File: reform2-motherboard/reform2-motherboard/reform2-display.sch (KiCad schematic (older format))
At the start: 5 parts, among them J2 EDP_30, U10 SN65DSI86ZQER

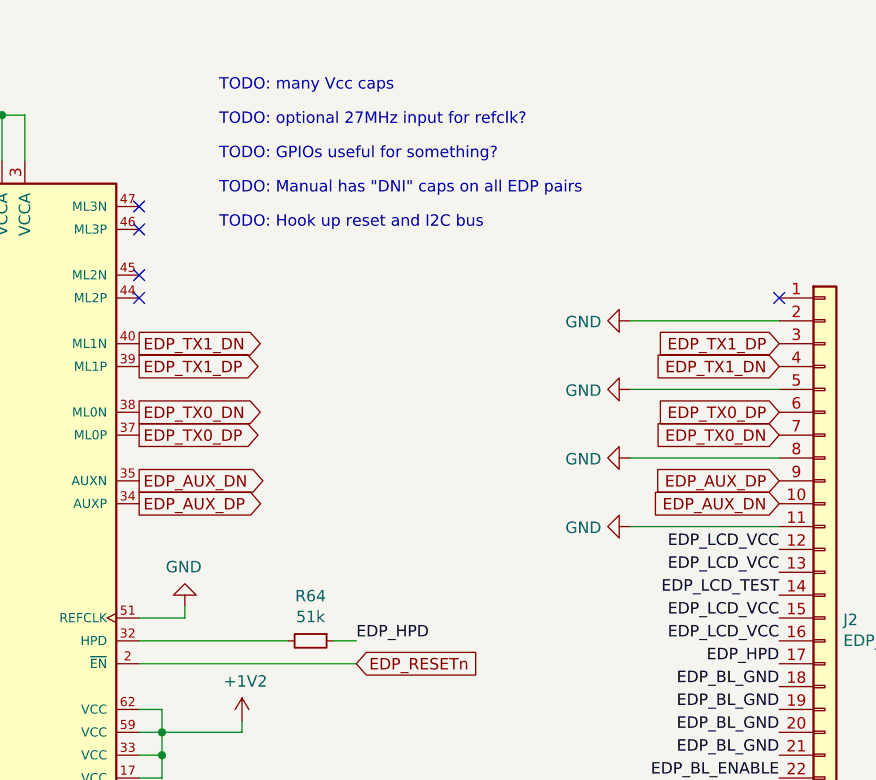
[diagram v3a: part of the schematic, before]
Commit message: WIP: reform2 schematic detail work all over the board and more footprints and 3d models added; changed one mpcie to M.2/NGFF/NVMe
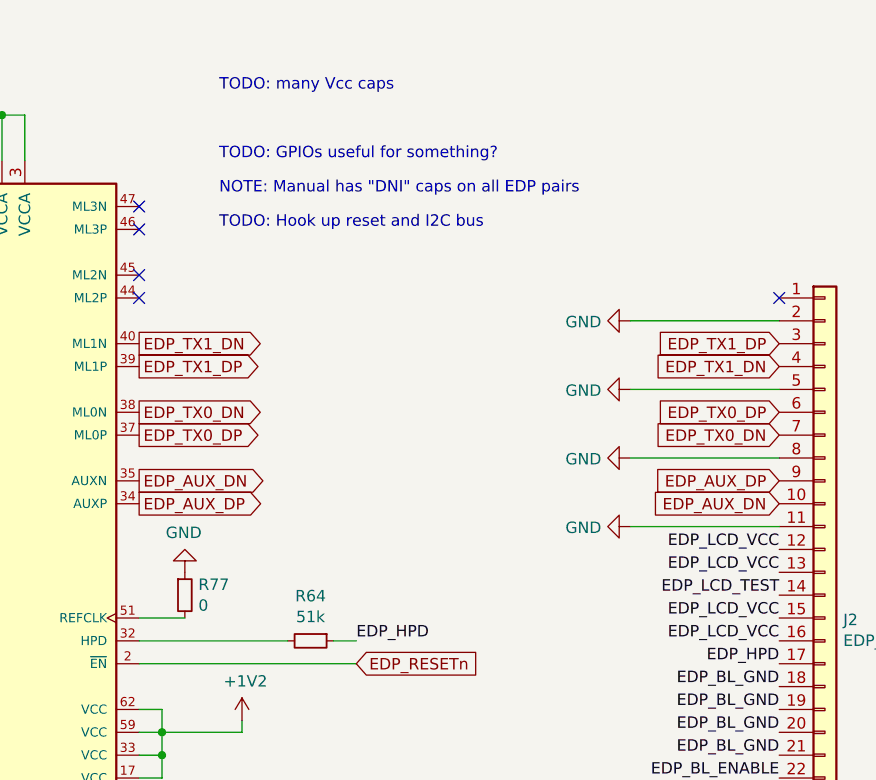
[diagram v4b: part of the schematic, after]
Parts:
- added R77: 0, Button_Switch_SMD:SW_Push_1P1T_NO_CK_KMR2, symbol Device:R_Small
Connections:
- net GND: now also R77.1; no longer U10.51 (REFCLK)
- new net: R77.2, U10.51 (REFCLK)
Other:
- note added: "NOTE: Manual has "DNI" caps on all EDP pairs"
- note removed: "TODO: Manual has "DNI" caps on all EDP pairs"
- note removed: "TODO: optional 27MHz input for refclk?"
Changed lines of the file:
@@
 L power:GND #PWR038
 U 1 1 5DAA7616
-P 6100 3600
-F 0 "#PWR038" H 6100 3350 50  0001 C CNN
-F 1 "GND" H 6105 3427 50  0000 C CNN
-F 2 "" H 6100 3600 50  0001 C CNN
-F 3 "" H 6100 3600 50  0001 C CNN
-	1    6100 3600
+P 6100 3450
+F 0 "#PWR038" H 6100 3200 50  0001 C CNN
+F 1 "GND" H 6105 3277 50  0000 C CNN
+F 2 "" H 6100 3450 50  0001 C CNN
+F 3 "" H 6100 3450 50  0001 C CNN
+	1    6100 3450
 	-1   0    0    1
 $EndComp
 Wire Wire Line
-	6100 3600 6100 3650
-Wire Wire Line
 	6100 3650 5900 3650
-Text Notes 6250 1500 0    50   ~ 0
-TODO: optional 27MHz input for refclk?
 Text GLabel 6850 3850 2    50   Input ~ 0
 EDP_RESETn
@@
 	7500 5050 6950 5050
 Text Notes 6250 1800 0    50   ~ 0
-TODO: Manual has "DNI" caps on all EDP pairs
+NOTE: Manual has "DNI" caps on all EDP pairs
 Text Notes 6250 1950 0    50   ~ 0
 TODO: Hook up reset and I2C bus
+$Comp
+L Device:R_Small R77
+U 1 1 60F2545C
+P 6100 3550
+F 0 "R77" H 6159 3596 50  0000 L CNN
+F 1 "0" H 6159 3505 50  0000 L CNN
+F 2 "Button_Switch_SMD:SW_Push_1P1T_NO_CK_KMR2" H 6100 3550 50  0001 C CNN
+F 3 "~" H 6100 3550 50  0001 C CNN
+	1    6100 3550
+	1    0    0    -1
+$EndComp
 $EndSCHEMATC

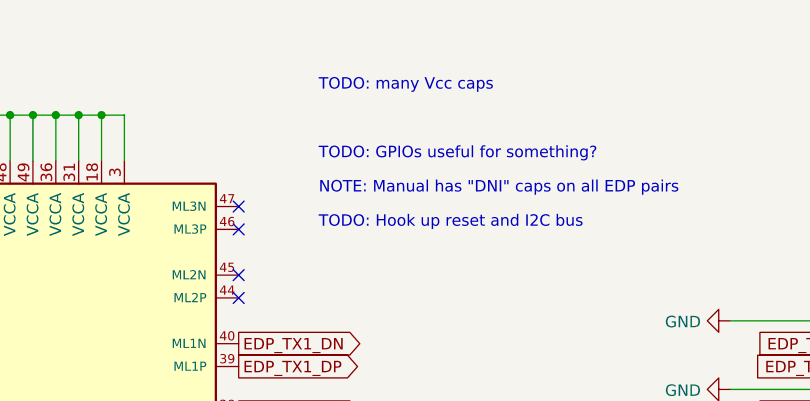
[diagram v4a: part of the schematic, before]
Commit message: WIP reform2: motherboard: many components sanity checked, passives footprints, fixed wrong NVMe/M.2 connector symbol and pins
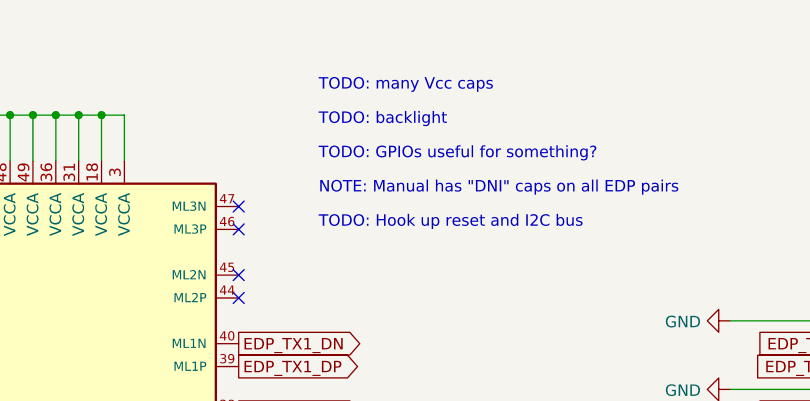
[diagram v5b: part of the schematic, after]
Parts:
- R77: footprint Button_Switch_SMD:SW_Push_1P1T_NO_CK_KMR2 -> Resistor_SMD:R_0603_1608Metric
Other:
- note added: "TODO: backlight"
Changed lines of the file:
@@
 F 0 "R77" H 6159 3596 50  0000 L CNN
 F 1 "0" H 6159 3505 50  0000 L CNN
-F 2 "Button_Switch_SMD:SW_Push_1P1T_NO_CK_KMR2" H 6100 3550 50  0001 C CNN
+F 2 "Resistor_SMD:R_0603_1608Metric" H 6100 3550 50  0001 C CNN
 F 3 "~" H 6100 3550 50  0001 C CNN
 	1    6100 3550
 	1    0    0    -1
 $EndComp
+Text Notes 6250 1500 0    50   ~ 0
+TODO: backlight
 $EndSCHEMATC

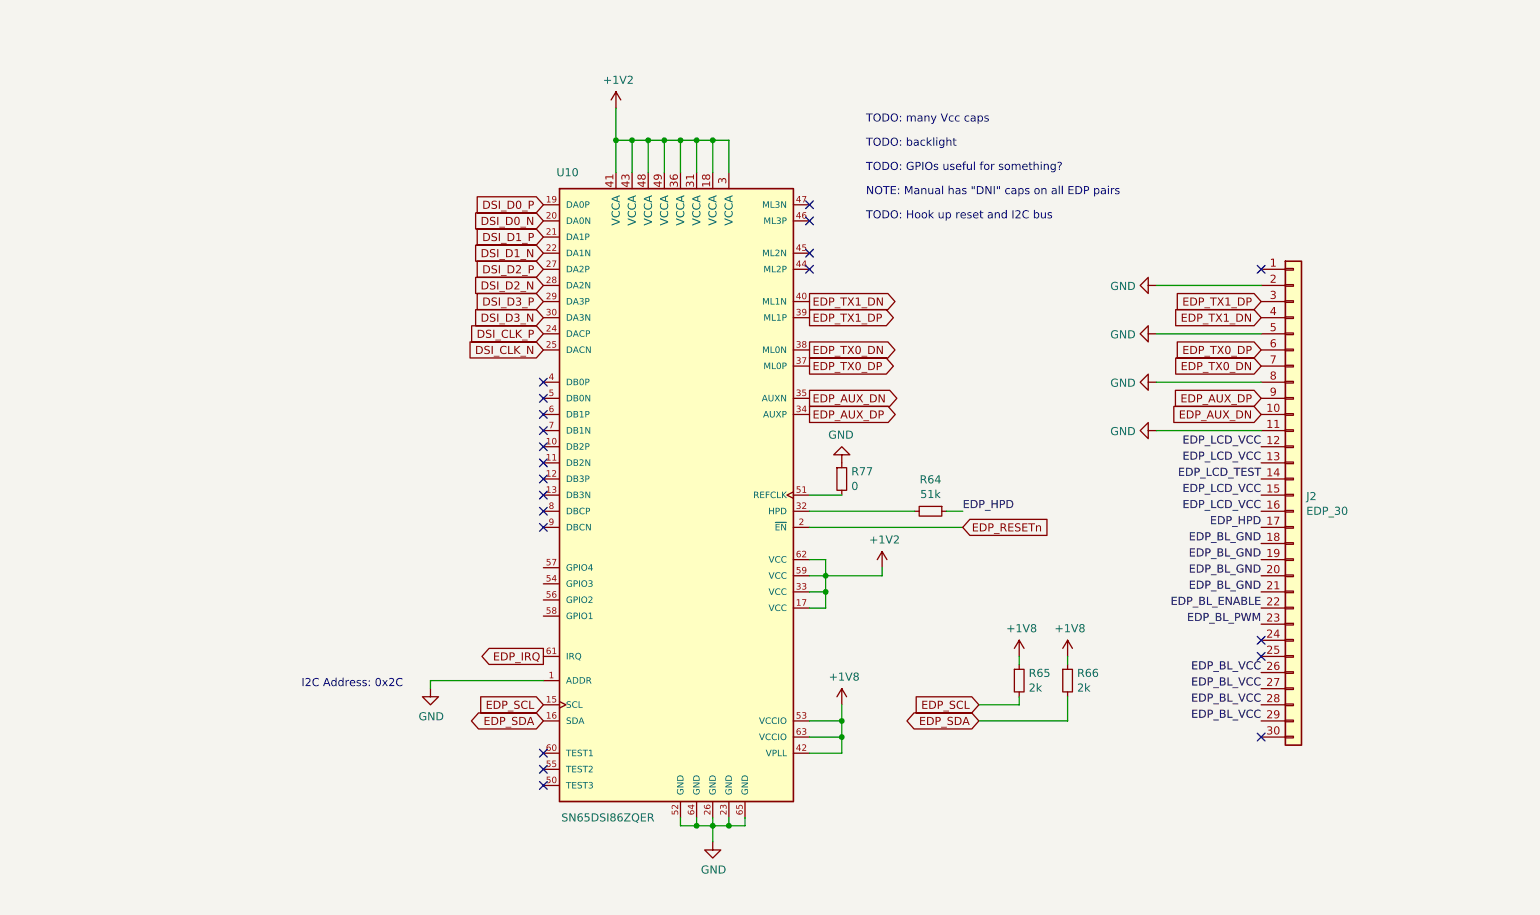
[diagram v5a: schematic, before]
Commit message: WIP: reform2 motherboard: eDP/eDP bridge caps
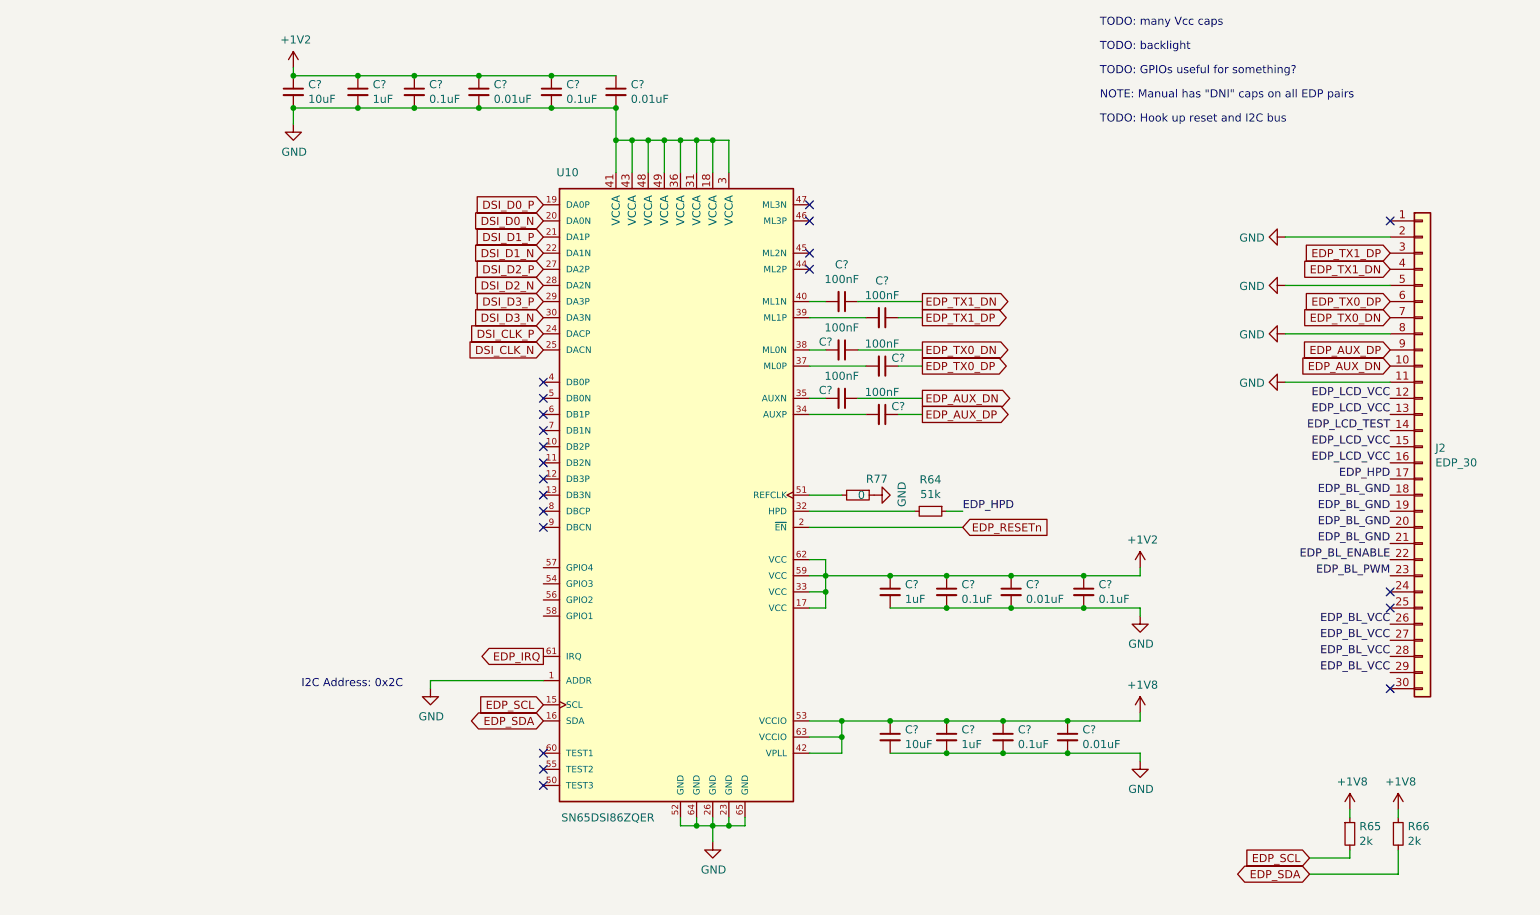
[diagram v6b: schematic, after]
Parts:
- added C? (x5): 0.1uF, symbol Device:C_Small
- added C? (x4): 0.01uF, symbol Device:C_Small
- added C? (x3): 1uF, symbol Device:C_Small
- added C? (x2): 10uF, symbol Device:C_Small
- added C? (x6): 100nF, symbol Device:C_Small
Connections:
- net +1V2: now also C?.1, C?.1, C?.1, C?.1, C?.1, C?.1, C?.1, C?.1, C?.1, C?.1; no longer U10.18 (VCCA), U10.3 (VCCA), U10.31 (VCCA), U10.36 (VCCA), U10.41 (VCCA), U10.43 (VCCA), U10.48 (VCCA), U10.49 (VCCA)
- net +1V8: now also C?.1, C?.1, C?.1, C?.1
- net EDP_AUX_DN: now also C?.1; no longer U10.35 (AUXN)
- net EDP_AUX_DP: now also C?.1; no longer U10.34 (AUXP)
- net EDP_TX0_DN: now also C?.1; no longer U10.38 (ML0N)
- net EDP_TX0_DP: now also C?.1; no longer U10.37 (ML0P)
- net EDP_TX1_DN: now also C?.1; no longer U10.40 (ML1N)
- net EDP_TX1_DP: now also C?.1; no longer U10.39 (ML1P)
- net GND: now also U10.18 (VCCA), U10.3 (VCCA), U10.31 (VCCA), U10.36 (VCCA), U10.41 (VCCA), U10.43 (VCCA), U10.48 (VCCA), U10.49 (VCCA), C?.2, C?.2, C?.2, C?.2, C?.2, C?.2, C?.2, C?.2, C?.2, C?.2, C?.2, C?.2, C?.2, C?.2
- new net: C?.2, U10.34 (AUXP)
- new net: C?.2, U10.35 (AUXN)
- new net: C?.2, U10.37 (ML0P)
- new net: C?.2, U10.38 (ML0N)
- new net: C?.2, U10.39 (ML1P)
- new net: C?.2, U10.40 (ML1N)
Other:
- moved on the sheet: J2, R65, R66, R77

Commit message: WIP: reform2 motherboard: more sanity and footprint checks, passives
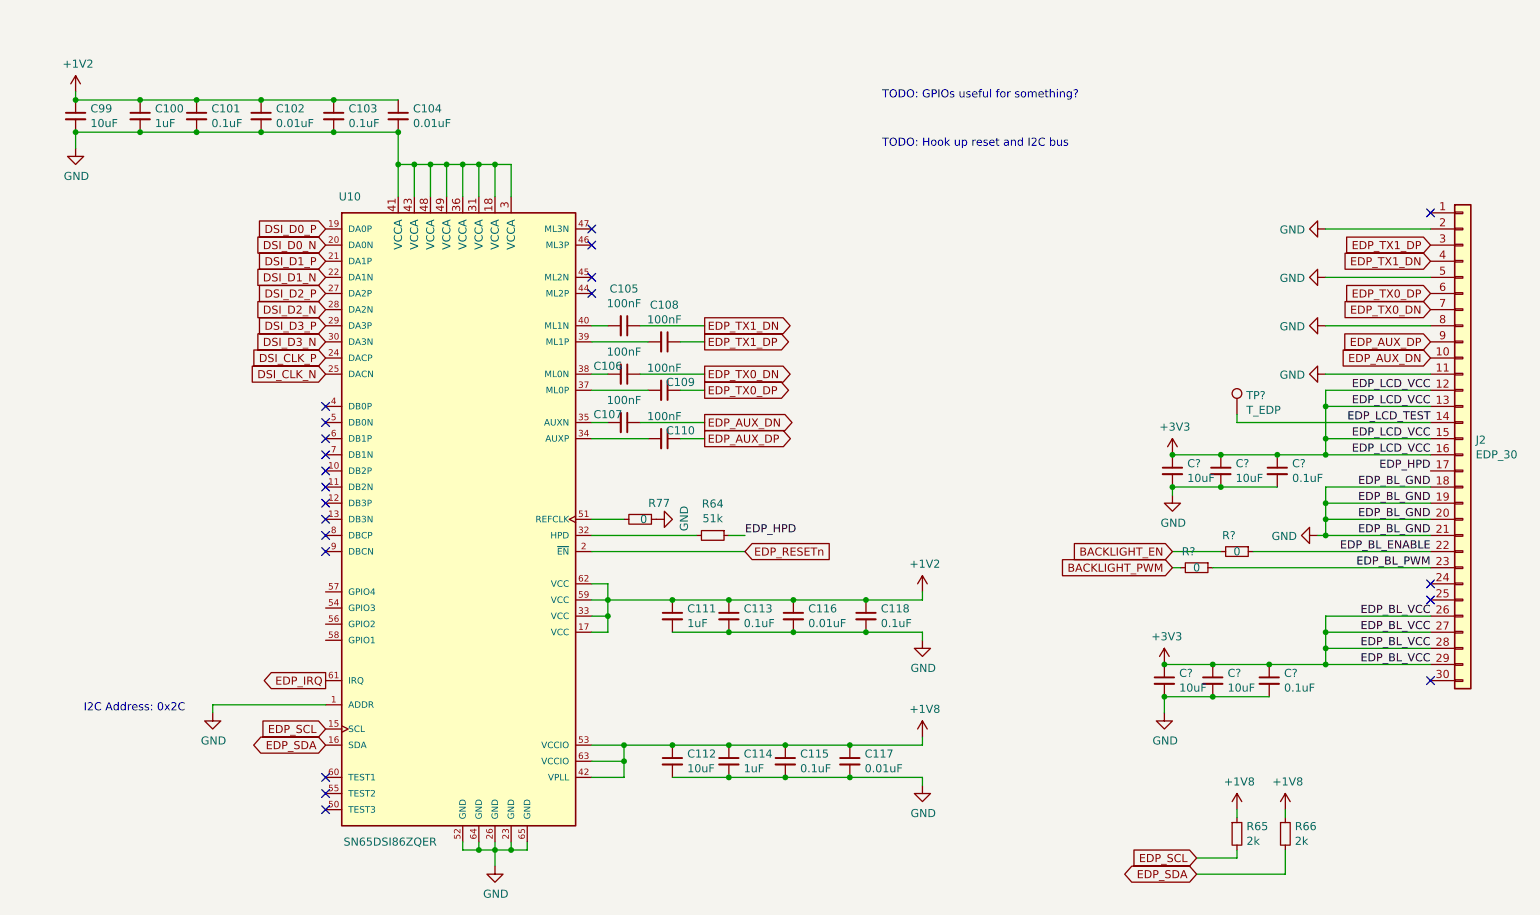
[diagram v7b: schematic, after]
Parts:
- added C? (x4): 10uF, symbol Device:C_Small
- added C? (x2): 0.1uF, symbol Device:C_Small
- added R? (x2): 0, symbol Device:R_Small
- added TP?: T_EDP, symbol Connector:TestPoint
- gave numbers to parts that had none: 20
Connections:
- net EDP_BL_GND is gone; now on net GND: J2.18 (Pin_18), J2.19 (Pin_19), J2.20 (Pin_20), J2.21 (Pin_21)
- net EDP_LCD_VCC is gone; now on net +3V3: J2.12 (Pin_12), J2.13 (Pin_13), J2.15 (Pin_15), J2.16 (Pin_16)
- net EDP_BL_ENABLE: now also R?.1
- net EDP_BL_PWM: now also R?.1
- net EDP_LCD_TEST: now also TP?.1
- net GND: now also C?.2, C?.2, C?.2, C?.2, C?.2, C?.2
- net EDP_BL_VCC renamed +3V3
- net +3V3: now also C?.1, C?.1, C?.1, C?.1, C?.1, C?.1
- new net BACKLIGHT_EN: R?.2
- new net BACKLIGHT_PWM: R?.2
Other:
- note removed: "NOTE: Manual has "DNI" caps on all EDP pairs"
- note removed: "TODO: backlight"
- note removed: "TODO: many Vcc caps"
- moved on the sheet: C100, C101, C102, C103, C104, C105, C106, C107, C108, C109, C110, C111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

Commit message: WIP: reform2 motherboard: more schematics tuning, preliminary selection of most components
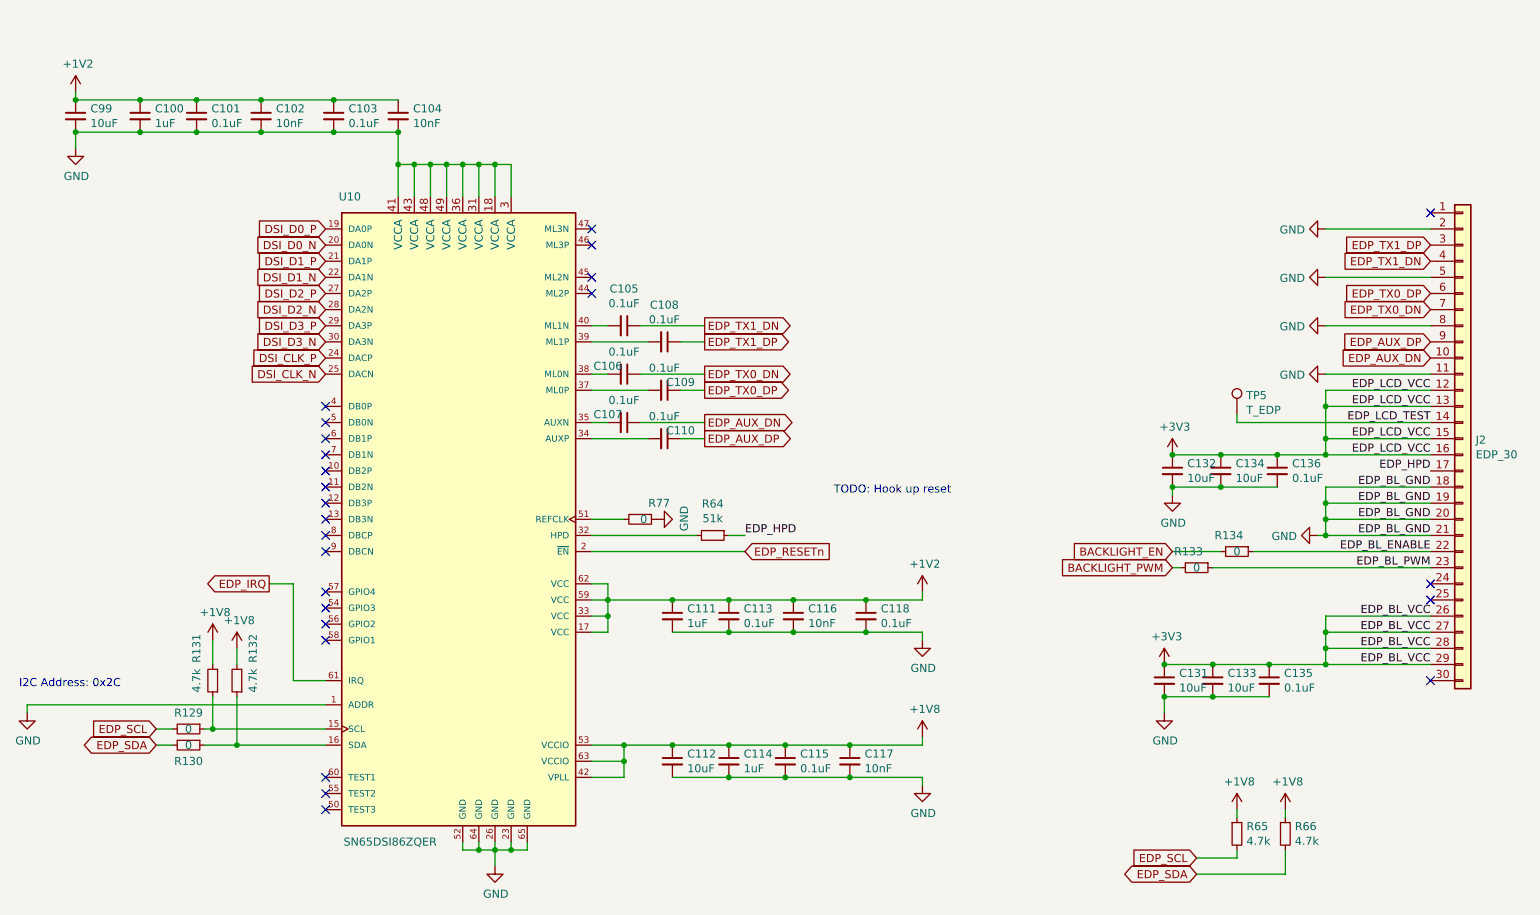
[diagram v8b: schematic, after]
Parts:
- added R129, R130: 0, Resistor_SMD:R_0603_1608Metric, symbol Device:R_Small
- added R131, R132: 4.7k, Resistor_SMD:R_0603_1608Metric, symbol Device:R_Small
- C100, C111, C114: footprint (none) -> Capacitor_SMD:C_0603_1608Metric; Manufacturer (none) -> Taiyo Yuden; Manufacturer_No (none) -> JMK107C6105KA
- C101, C103, C113, C115, C118: footprint (none) -> Capacitor_SMD:C_0603_1608Metric; Manufacturer (none) -> TDK; Manufacturer_No (none) -> CGA3E2X8R1E104K080AE
- C102, C104, C116, C117: value 0.01uF -> 10nF; footprint (none) -> Capacitor_SMD:C_0603_1608Metric; Manufacturer (none) -> KEMET; Manufacturer_No (none) -> C0603C103K5RAC3190
- C105, C106, C107, C108, C109, C110: value 100nF -> 0.1uF; footprint (none) -> Capacitor_SMD:C_0603_1608Metric; Manufacturer (none) -> TDK; Manufacturer_No (none) -> CGA3E2X8R1E104K080AE
- C112, C99: footprint (none) -> Capacitor_SMD:C_0603_1608Metric; Manufacturer (none) -> Taiyo Yuden; Manufacturer_No (none) -> LMK107BBJ106KALT
- C131, C132, C133, C134: renamed from C?; footprint (none) -> Capacitor_SMD:C_0603_1608Metric; Manufacturer (none) -> Taiyo Yuden; Manufacturer_No (none) -> LMK107BBJ106KALT
- C135, C136: renamed from C?; footprint (none) -> Capacitor_SMD:C_0603_1608Metric; Manufacturer (none) -> TDK; Manufacturer_No (none) -> CGA3E2X8R1E104K080AE
- J2: Manufacturer (none) -> Hirose; Manufacturer_No (none) -> FH12-30S-0.5SH(55)
- R133, R134: renamed from R?; footprint (none) -> Resistor_SMD:R_0603_1608Metric; Manufacturer (none) -> Vishay Dale; Manufacturer_No (none) -> CRCW06030000Z0EAC
- R65, R66: value 2k -> 4.7k; Manufacturer (none) -> Yageo; Manufacturer_No (none) -> RC0603FR-074K7L
- R77: Manufacturer (none) -> Vishay Dale; Manufacturer_No (none) -> CRCW06030000Z0EAC
- TP5: renamed from TP?; footprint (none) -> TestPoint:TestPoint_Pad_1.0x1.0mm
- U10: Manufacturer (none) -> Texas Instruments; Manufacturer_No (none) -> SN65DSI86ZQER
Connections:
- net +1V8: now also R131.2, R132.2
- net EDP_SCL: now also R129.2; no longer U10.15 (SCL)
- net EDP_SDA: now also R130.2; no longer U10.16 (SDA)
- new net: R129.1, R131.1, U10.15 (SCL)
- new net: R130.1, R132.1, U10.16 (SDA)
- no-connect marks 21 -> 25
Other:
- note added: "TODO: Hook up reset"
- note removed: "TODO: GPIOs useful for something?"
- note removed: "TODO: Hook up reset and I2C bus"
